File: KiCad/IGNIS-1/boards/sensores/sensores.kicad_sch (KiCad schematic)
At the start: 11 parts, among them J41 Backplane_2x10, U20 BME280, U21 MPU6050, U22 MQ-135, U24 GPS NEO-6M

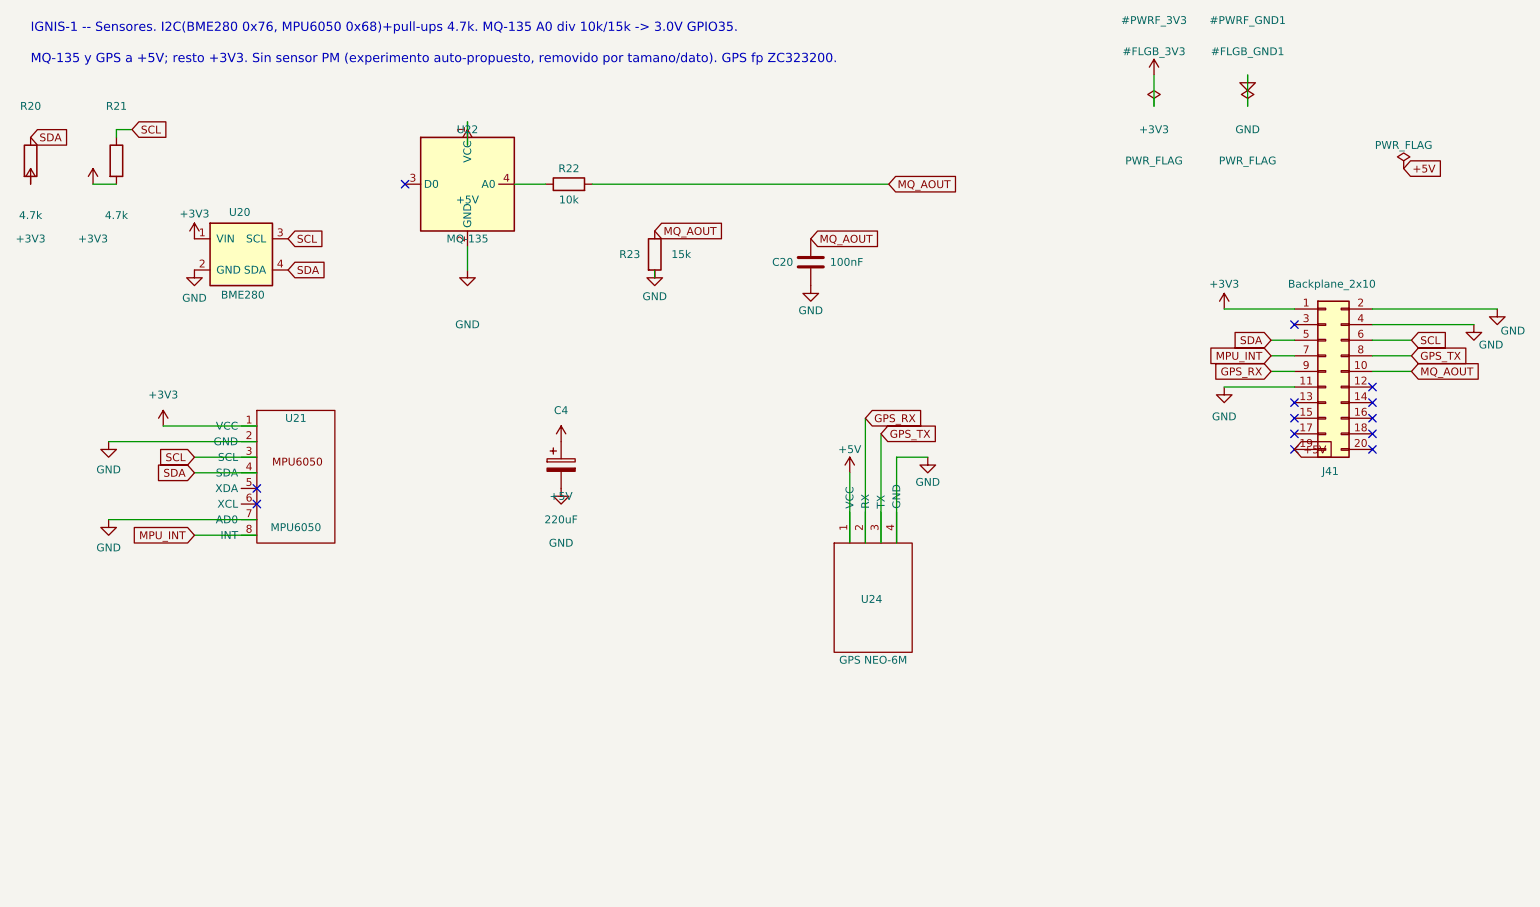
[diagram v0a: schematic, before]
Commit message: 5 boards separados, falta ajustar dimensiones de BME280 y MQ-135
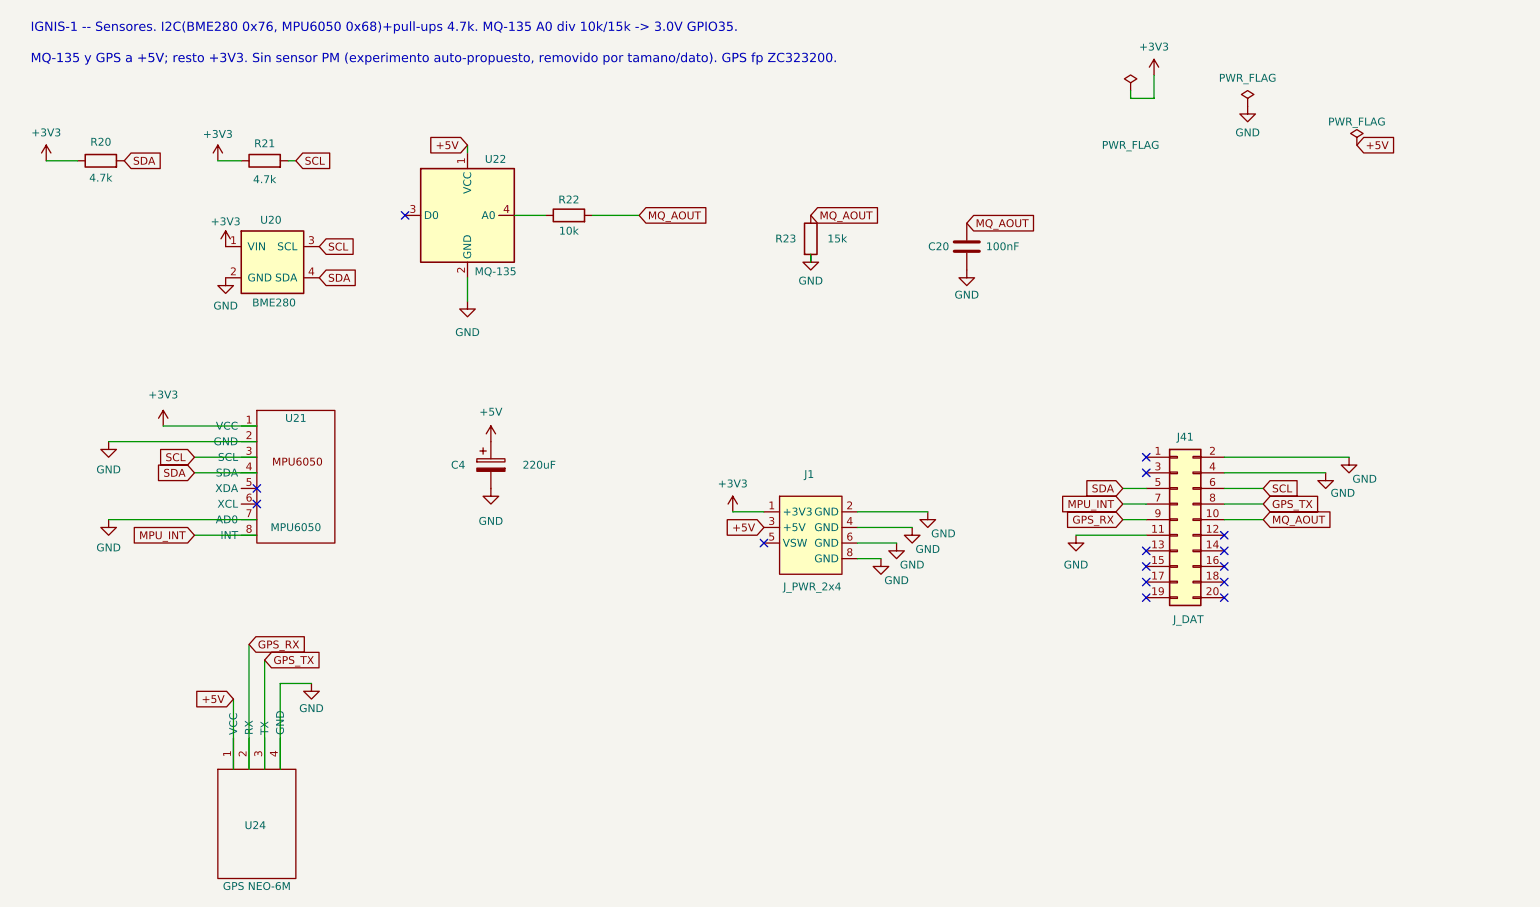
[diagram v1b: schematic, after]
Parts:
- added J1: J_PWR_2x4, IGNIS1:J_PWR_2x4_Keyed, symbol IGNIS1:J_PWR_2x4
- J41: value Backplane_2x10 -> J_DAT
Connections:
- net +3V3: now also R20.1, R21.1, J1.1 (+3V3); no longer J41.1 (Pin_1), R20.2, R21.2
- net +5V: now also J1.3 (+5V); no longer J41.19 (Pin_19)
- net GND: now also J1.2 (GND), J1.4 (GND), J1.6 (GND), J1.8 (GND)
- net SCL: now also R21.2; no longer R21.1
- net SDA: now also R20.2; no longer R20.1
- no-connect marks 13 -> 15
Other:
- moved on the sheet: C20, C4, J41, R20, R21, R22, R23, U20, U22, U24
